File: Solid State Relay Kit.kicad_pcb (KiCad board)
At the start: 2 copper layers, 25.8 x 21 mm, 11 parts, among them J1 Conn_01x03, J2 Conn_01x02, Q1 2N3904, U1 S108T02

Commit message: update,
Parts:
- D1, D2: footprint LEDs:LED_0805_HandSoldering -> LED_SMD:LED_0805_2012Metric_Pad1.15x1.40mm_HandSolder
- J1: footprint footprint-lib:Pin_Header_Straight_1x03_Pitch2.54mm -> footprint-lib.pretty:Pin_Header_Straight_1x03_Pitch2.54mm
- Q1: footprint TO_SOT_Packages_SMD:TSOT-23_HandSoldering -> Package_TO_SOT_SMD:TSOT-23_HandSoldering
- R1, R2, R3, R4, R5: footprint Resistors_SMD:R_0805_HandSoldering -> footprint-lib.pretty:R_0805_HandSoldering

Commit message: update,
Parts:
- added REF**: MountingHole_3.2mm_M3, MountingHole:MountingHole_3.2mm_M3, F.Cu at (33.0, 21.6)
- added REF**: MountingHole_3.2mm_M3, MountingHole:MountingHole_3.2mm_M3, F.Cu at (33.0, 50.8)
- added REF**: MountingHole_3.2mm_M3, MountingHole:MountingHole_3.2mm_M3, F.Cu at (62.2, 21.6)
- added REF**: MountingHole_3.2mm_M3, MountingHole:MountingHole_3.2mm_M3, F.Cu at (62.2, 50.8)
- D1, D2: footprint LED_SMD:LED_0805_2012Metric_Pad1.15x1.40mm_HandSolder -> LED_SMD:LED_0805_2012Metric_Castellated
- J1: footprint footprint-lib.pretty:Pin_Header_Straight_1x03_Pitch2.54mm -> Connector_PinHeader_2.54mm:PinHeader_1x03_P2.54mm_Vertical
- J2: footprint Connectors_Phoenix:PhoenixContact_MCV-G_02x5.08mm_Vertical -> w_conn_mpt:mpt_0,5%2f2-2,54
- R1, R2, R3, R4, R5: footprint footprint-lib.pretty:R_0805_HandSoldering -> Resistor_SMD:R_0805_2012Metric_Pad1.15x1.40mm_HandSolder
- U1: footprint Housings_SIP:SIP4_Sharp-SSR_Pitch7.62mm_Straight -> footprint-lib:OMRON-G3MB-202P
- moved U1 18.5 mm to (55.9, 36.6), turned to 90 degrees
- moved D2 13.3 mm to (44.4, 41.3)
- moved R3 13.3 mm to (48.4, 42.1)
- moved R4 13.3 mm to (44.4, 36.3)
- moved R5 13.3 mm to (44.4, 44.0)
- moved R1 13.3 mm to (44.3, 34.1)
- moved R2 13.3 mm to (44.3, 31.9)
- moved D1 13.3 mm to (44.4, 39.0)
- moved Q1 13.3 mm to (49.1, 33.7)
- moved J1 10.5 mm to (32.0, 43.0)
- moved J2 8.29 mm to (33.5, 29.0), turned to 270 degrees
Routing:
- net GND: track 41.3 -> 49.6 mm
- net /SSR_OUT2: track 19.1 -> 24.4 mm
- net /SSR_IN1: track 19.7 -> 23.7 mm
- net /SSR_OUT1: track 22.1 -> 25.4 mm
- net +5V: track 13.6 -> 16.5 mm
- net /SSR_IN2: track 13.6 -> 16.4 mm
- net /SIG_CONTROL: track 12.3 -> 14.4 mm
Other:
- board size 25.8 x 21 mm -> 36.3 x 36.3 mm

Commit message: update,
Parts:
- added 5V1: TestPoint, TestPoint:TestPoint_Loop_D1.80mm_Drill1.0mm_Beaded, F.Cu at (49.5, 50.8)
- added C1: 105, Capacitor_SMD:CP_Elec_4x3, F.Cu at (36.6, 43.5)
- added D3: LED, LED_SMD:LED_0805_2012Metric_Castellated, F.Cu at (49.8, 46.4)
- added GND1: TestPoint, TestPoint:TestPoint_Loop_D1.80mm_Drill1.0mm_Beaded, F.Cu at (54.6, 50.8)
- added Q2: 2N3904, Package_TO_SOT_SMD:TSOT-23_HandSoldering, F.Cu at (55.2, 36.8)
- added R6: 331, Resistor_SMD:R_0805_2012Metric_Pad1.15x1.40mm_HandSolder, F.Cu at (49.8, 38.6)
- added R7: 103, Resistor_SMD:R_0805_2012Metric_Pad1.15x1.40mm_HandSolder, F.Cu at (49.8, 35.9)
- added R8: 331, Resistor_SMD:R_0805_2012Metric_Pad1.15x1.40mm_HandSolder, F.Cu at (49.8, 44.2)
- added R9: 680, Resistor_SMD:R_0805_2012Metric_Pad1.15x1.40mm_HandSolder, F.Cu at (49.8, 41.3)
- added SSR1: TestPoint, TestPoint:TestPoint_Loop_D1.80mm_Drill1.0mm_Beaded, F.Cu at (39.4, 50.9)
- added SSR2: TestPoint, TestPoint:TestPoint_Loop_D1.80mm_Drill1.0mm_Beaded, F.Cu at (44.5, 50.8)
- added U2: OMRON G3MB-202P, footprint-lib:OMRON-G3MB-202P, F.Cu at (50.0, 28.4)
- J1: footprint Connector_PinHeader_2.54mm:PinHeader_1x03_P2.54mm_Vertical -> Connector_PinHeader_2.54mm:PinHeader_1x04_P2.54mm_Vertical
- J2: value Conn_01x02 -> SSR_OUTPUT; footprint w_conn_mpt:mpt_0,5%2f2-2,54 -> w_conn_mpt:mpt_0,5%2f4-2,54
- R4: value 331 -> 680
- U1: value S108T02 -> OMRON G3MB-202P
- moved J2 35.4 mm to (67.3, 39.4), turned to 90 degrees
- moved R5 17.8 mm to (34.1, 29.5), turned to 270 degrees
- moved D2 17.6 mm to (31.4, 29.5), turned to 270 degrees
- moved U1 16.3 mm to (50.0, 21.3), turned to 0 degrees
- moved D1 7.31 mm to (43.5, 46.3)
- moved R1 6.88 mm to (39.2, 38.7)
- moved R2 6.64 mm to (39.2, 36.2)
- moved Q1 5.54 mm to (44.6, 36.8)
- moved R4 5.54 mm to (41.8, 41.2)
- moved REF** 5.33 mm to (67.6, 21.6)
- moved REF** 5.33 mm to (67.6, 50.8)
- moved R3 5.13 mm to (43.6, 43.8), turned to 180 degrees
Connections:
- net /SIG_CONTROL renamed /SSR_CONTROL1
- net /SSR_IN1 renamed /SSR1_IN1
- net /SSR_IN2 renamed /SSR1_IN2
- J2 pad 1: /SSR_OUT1 -> /SSR1_OUT2
- J2 pad 2: /SSR_OUT2 -> /SSR1_OUT1
- U1 pad 1: /SSR_OUT2 -> /SSR1_OUT2
- U1 pad 2: /SSR_OUT1 -> /SSR1_OUT1
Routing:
- net /SSR2_IN1: track 0.00 -> 39.1 mm, vias 0 -> 1
- net +5V: track 16.5 -> 52.6 mm
- net /SSR_CONTROL2: track 0.00 -> 32.1 mm, vias 0 -> 1
- net /SSR1_OUT1: track 0.00 -> 27.5 mm
- net /SSR_OUT1: track 25.4 -> 0.00 mm
- net /SSR_OUT2: track 24.4 -> 0.00 mm
- net /SSR2_OUT1: track 0.00 -> 23.5 mm
- net /SSR2_IN2: track 0.00 -> 19.8 mm, vias 0 -> 1
- net GND: track 49.6 -> 30.4 mm, vias 1 -> 4
- net /SSR1_OUT2: track 0.00 -> 16.9 mm
- net /SSR2_OUT2: track 0.00 -> 15.2 mm
- net /SSR_CONTROL1: track 14.4 -> 25.7 mm
- net Net-(Q2-Pad2): track 0.00 -> 10.9 mm
- net /SSR1_IN2: track 16.4 -> 26.6 mm
- net /SSR1_IN1: track 23.7 -> 31.2 mm
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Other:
- board size 36.3 x 36.3 mm -> 41.7 x 36.3 mm
- net class GND: via_dia 1 -> 1.4
- board text added: "MCU RELAY CONTROL BOARD"
- board text added: "ON = CLOSED OFF = OPEN"
- board text added: "PWR"
- board text added: "SSR1"
- board text added: "SSR2"

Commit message: update comment,
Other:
- board text added: "MCU RELAY CONTROL BOARD louiscklaw@gmail.com"
- board text removed: "MCU RELAY CONTROL BOARD"
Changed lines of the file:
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@@
     (pad 1 np_thru_hole circle (at 0 0) (size 3.2 3.2) (drill 3.2) (layers *.Cu *.Mask))
   )
-  (gr_text "MCU RELAY \nCONTROL BOARD" (at 62.484 34.8234) (layer B.SilkS)
-    (effects (font (size 1.5 1.5) (thickness 0.3)) (justify left mirror))
+  (gr_text "MCU RELAY \nCONTROL BOARD\n\nlouiscklaw@gmail.com" (at 62.738 38.608) (layer B.SilkS)
+    (effects (font (size 1.5 1.5) (thickness 0.2)) (justify left mirror))
   )
   (gr_text "ON = CLOSED\nOFF = OPEN" (at 59.7408 53.721 90) (layer F.SilkS)

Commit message: start panelizing,
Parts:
- removed the REF** at (33.0, 21.6)
- removed the REF** at (33.0, 50.8)
- removed the REF** at (67.6, 21.6)
- removed the REF** at (67.6, 50.8)
- added REF**: MountingHole_3.2mm_M3, MountingHole:MountingHole_3.2mm_M3, F.Cu at (5.02, 5.59)
- added REF**: MountingHole_3.2mm_M3, MountingHole:MountingHole_3.2mm_M3, F.Cu at (5.02, 34.8)
- added REF**: MountingHole_3.2mm_M3, MountingHole:MountingHole_3.2mm_M3, F.Cu at (39.6, 5.59)
- added REF**: MountingHole_3.2mm_M3, MountingHole:MountingHole_3.2mm_M3, F.Cu at (39.6, 34.8)
- moved SSR2 32.2 mm to (16.4, 34.8)
- moved 5V1 32.2 mm to (21.5, 34.8)
- moved C1 32.2 mm to (8.60, 27.5)
- moved D1 32.2 mm to (15.5, 30.3)
- moved D2 32.2 mm to (3.40, 13.5)
- moved D3 32.2 mm to (21.8, 30.4)
- moved GND1 32.2 mm to (26.6, 34.8)
- moved J1 32.2 mm to (4.00, 27.0)
- moved J2 32.2 mm to (39.3, 23.4)
- moved Q1 32.2 mm to (16.6, 20.8)
- moved Q2 32.2 mm to (27.2, 20.8)
- moved R1 32.2 mm to (11.2, 22.7)
- moved R2 32.2 mm to (11.2, 20.2)
- moved R3 32.2 mm to (15.6, 27.8)
- moved R4 32.2 mm to (13.8, 25.2)
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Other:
- board size 41.7 x 36.3 mm -> 90 x 90 mm

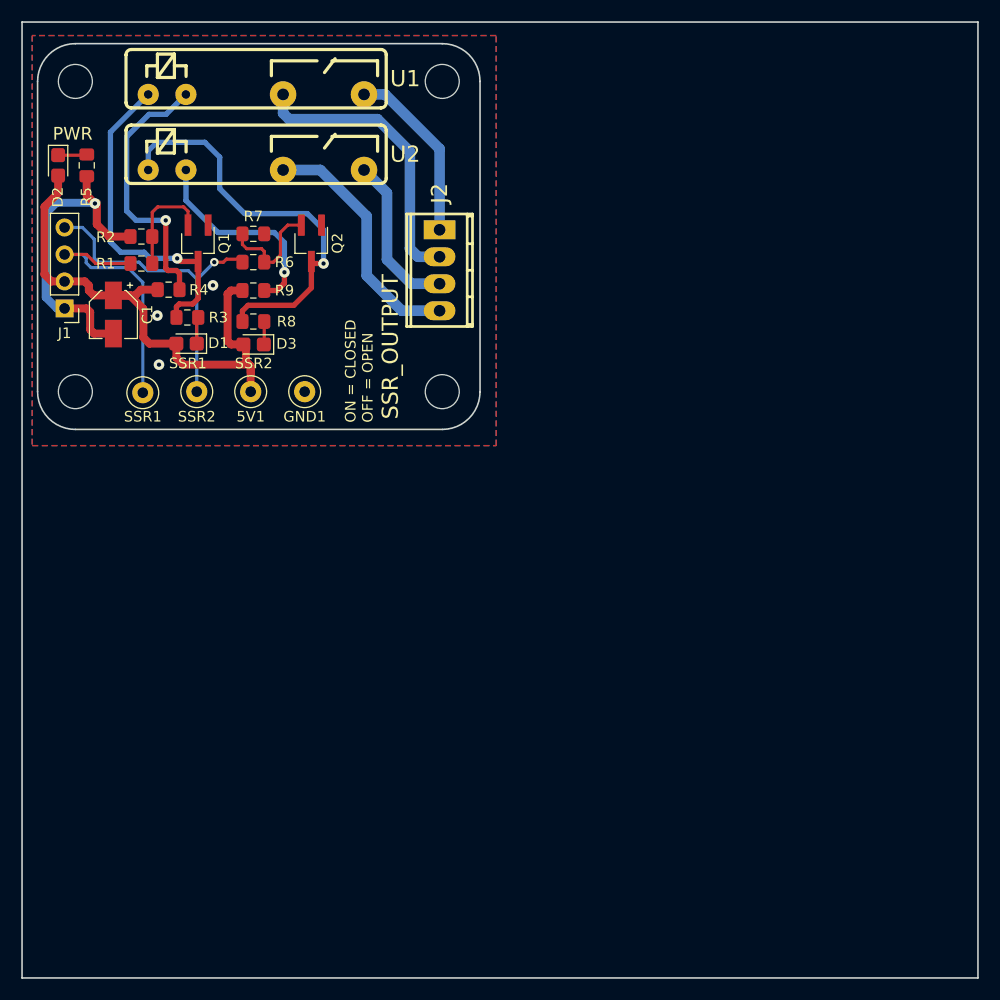
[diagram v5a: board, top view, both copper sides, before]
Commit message: simplify tracks,.
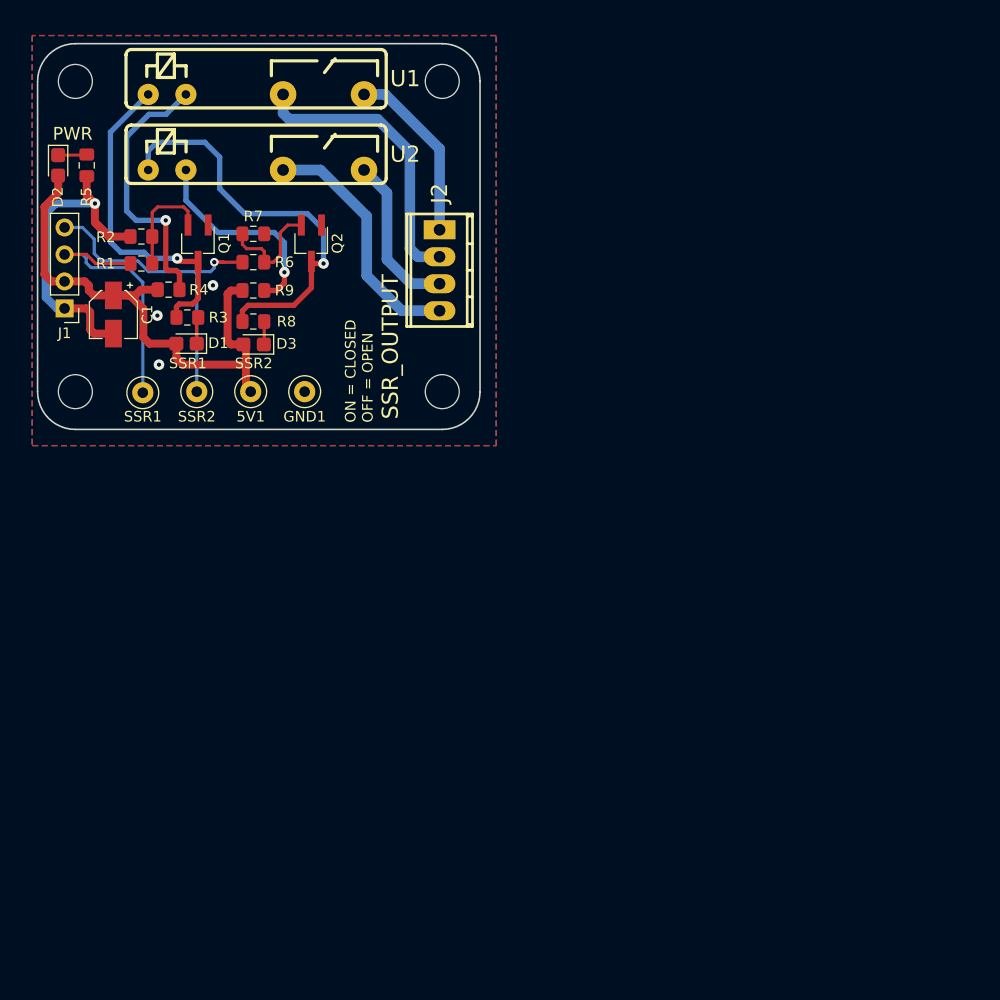
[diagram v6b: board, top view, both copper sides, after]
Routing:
- net GND: track 30.4 -> 31.9 mm
- net +5V: track 52.6 -> 51.6 mm
- net /SSR_CONTROL2: track 32.1 -> 33.0 mm
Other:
- board size 90 x 90 mm -> 41.7 x 36.3 mm
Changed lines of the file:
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@@
   (general
     (thickness 1.6)
-    (drawings 19)
-    (tracks 177)
+    (drawings 13)
+    (tracks 179)
     (zones 0)
     (modules 27)
@@
     (zone_45_only no)
     (trace_min 0.2)
-    (segment_width 0.2)
+    (segment_width 0.15)
     (edge_width 0.15)
     (via_size 0.8)
@@
     (pad 1 np_thru_hole circle (at 0 0) (size 3.2 3.2) (drill 3.2) (layers *.Cu *.Mask))
   )
-  (dimension 90 (width 0.3) (layer Dwgs.User)
-    (gr_text "90.000 mm" (at -5.1 45 270) (layer Dwgs.User)
-      (effects (font (size 1.5 1.5) (thickness 0.3)))
-    )
-    (feature1 (pts (xy 0 90) (xy -3.586421 90)))
-    (feature2 (pts (xy 0 0) (xy -3.586421 0)))
-    (crossbar (pts (xy -3 0) (xy -3 90)))
-    (arrow1a (pts (xy -3 90) (xy -3.586421 88.873496)))
-    (arrow1b (pts (xy -3 90) (xy -2.413579 88.873496)))
-    (arrow2a (pts (xy -3 0) (xy -3.586421 1.126504)))
-    (arrow2b (pts (xy -3 0) (xy -2.413579 1.126504)))
-  )
-  (dimension 90 (width 0.3) (layer Dwgs.User)
-    (gr_text "90.000 mm" (at 45 -5.1) (layer Dwgs.User)
-      (effects (font (size 1.5 1.5) (thickness 0.3)))
-    )
-    (feature1 (pts (xy 90 0) (xy 90 -3.586421)))
-    (feature2 (pts (xy 0 0) (xy 0 -3.586421)))
-    (crossbar (pts (xy 0 -3) (xy 90 -3)))
-    (arrow1a (pts (xy 90 -3) (xy 88.873496 -2.413579)))
-    (arrow1b (pts (xy 90 -3) (xy 88.873496 -3.586421)))
-    (arrow2a (pts (xy 0 -3) (xy 1.126504 -2.413579)))
-    (arrow2b (pts (xy 0 -3) (xy 1.126504 -3.586421)))
-  )
-  (gr_line (start 0 90) (end 0 0) (layer Edge.Cuts) (width 0.15))
-  (gr_line (start 90 90) (end 0 90) (layer Edge.Cuts) (width 0.15))
-  (gr_line (start 90 0) (end 90 90) (layer Edge.Cuts) (width 0.15))
-  (gr_line (start 0 0) (end 90 0) (layer Edge.Cuts) (width 0.15))
   (gr_text "MCU RELAY \nCONTROL BOARD\n\nlouiscklaw@gmail.com" (at 34.738 22.608) (layer B.SilkS)
     (effects (font (size 1.5 1.5) (thickness 0.2)) (justify left mirror))
@@
   (segment (start 6.29 25.275) (end 6.29 24.8034) (width 0.75) (layer F.Cu) (net 1))
   (segment (start 4.004 24.4224) (end 5.909 24.4224) (width 0.75) (layer F.Cu) (net 1))
-  (segment (start 21.53 34.8) (end 21.53 33.022) (width 0.75) (layer F.Cu) (net 1))
-  (segment (start 15.18 32.26) (end 14.525 31.605) (width 0.75) (layer F.Cu) (net 1))
-  (segment (start 21.276 32.26) (end 15.18 32.26) (width 0.75) (layer F.Cu) (net 1))
-  (segment (start 14.525 31.605) (end 14.525 30.2788) (width 0.75) (layer F.Cu) (net 1))
-  (segment (start 21.53 33.022) (end 21.53 32.514) (width 0.75) (layer F.Cu) (net 1))
-  (segment (start 21.53 32.514) (end 21.276 32.26) (width 0.75) (layer F.Cu) (net 1))
   (segment (start 2.11401 23.76601) (end 2.7704 24.4224) (width 0.75) (layer F.Cu) (net 1))
   (segment (start 2.7704 24.4224) (end 4.004 24.4224) (width 0.75) (layer F.Cu) (net 1))
@@
   (segment (start 3.39792 14.457044) (end 3.39792 16.10208) (width 0.75) (layer F.Cu) (net 1))
   (segment (start 3.39792 16.10208) (end 2.11401 17.38599) (width 0.75) (layer F.Cu) (net 1))
-  (segment (start 21.53 32.387) (end 21.0755 31.9325) (width 0.75) (layer F.Cu) (net 1))
-  (segment (start 21.53 33.022) (end 21.53 32.387) (width 0.75) (layer F.Cu) (net 1))
   (segment (start 21.0755 31.9325) (end 21.0755 30.355) (width 0.75) (layer F.Cu) (net 1))
   (segment (start 19.6758 25.275) (end 20.75 25.275) (width 0.75) (layer F.Cu) (net 1))
@@
   (segment (start 8.6014 25.7356) (end 10.1514 25.7356) (width 0.75) (layer F.Cu) (net 1))
   (segment (start 10.1514 25.7356) (end 11.4208 27.005) (width 0.75) (layer F.Cu) (net 1))
+  (segment (start 21.0755 34.3455) (end 21.53 34.8) (width 0.75) (layer F.Cu) (net 1))
+  (segment (start 14.525 31.605) (end 15.18 32.26) (width 0.75) (layer F.Cu) (net 1))
+  (segment (start 14.525 30.2788) (end 14.525 31.605) (width 0.75) (layer F.Cu) (net 1))
+  (segment (start 21.0655 32.26) (end 21.0755 32.25) (width 0.75) (layer F.Cu) (net 1))
+  (segment (start 15.18 32.26) (end 21.0655 32.26) (width 0.75) (layer F.Cu) (net 1))
+  (segment (start 21.0755 31.9325) (end 21.0755 32.25) (width 0.75) (layer F.Cu) (net 1))
+  (segment (start 21.0755 32.25) (end 21.0755 34.3455) (width 0.75) (layer F.Cu) (net 1))
   (segment (start 16.45 27.2308) (end 16.45 29.748366) (width 0.3) (layer F.Cu) (net 2) (status 30))
   (segment (start 16.45 29.748366) (end 16.5825 29.880866) (width 0.3) (layer F.Cu) (net 2) (status 30))
   (segment (start 10.209 20.195) (end 8.195 20.195) (width 0.75) (layer F.Cu) (net 3))
-  (segment (start 7.034 19.034) (end 7.034 17.02) (width 0.75) (layer F.Cu) (net 3))
   (segment (start 8.195 20.195) (end 7.034 19.034) (width 0.75) (layer F.Cu) (net 3))
   (segment (start 6.7946 29.3356) (end 8.6014 29.3356) (width 0.75) (layer F.Cu) (net 3))
@@
   (segment (start 4.004 26.9624) (end 3.2784 26.9624) (width 0.75) (layer B.Cu) (net 3))
   (segment (start 3.2784 26.9624) (end 2.226 25.91) (width 0.75) (layer B.Cu) (net 3))
-  (segment (start 3.242 17.02) (end 2.226 18.036) (width 0.75) (layer B.Cu) (net 3))
   (segment (start 2.226 25.91) (end 2.226 18.036) (width 0.75) (layer B.Cu) (net 3))
-  (segment (start 7.052 17.02) (end 3.242 17.02) (width 0.75) (layer B.Cu) (net 3))
   (via (at 12.894 32.26) (size 1) (drill 0.4) (layers F.Cu B.Cu) (net 3))
-  (segment (start 7.034 17.02) (end 7.034 17.02) (width 0.75) (layer F.Cu) (net 3))
   (segment (start 6.09032 16.31232) (end 6.8615 17.0835) (width 0.75) (layer F.Cu) (net 3))
   (segment (start 6.09032 14.519544) (end 6.09032 16.31232) (width 0.75) (layer F.Cu) (net 3))
@@
   (via (at 17.974 24.7924) (size 1) (drill 0.4) (layers F.Cu B.Cu) (net 3))
   (via (at 12.7416 27.6372) (size 1) (drill 0.4) (layers F.Cu B.Cu) (net 3))
+  (segment (start 6.8615 18.8615) (end 8.195 20.195) (width 0.75) (layer F.Cu) (net 3))
+  (segment (start 6.8615 17.0835) (end 6.8615 18.8615) (width 0.75) (layer F.Cu) (net 3))
+  (segment (start 3.1785 17.0835) (end 2.226 18.036) (width 0.75) (layer B.Cu) (net 3))
+  (segment (start 6.8615 17.0835) (end 3.1785 17.0835) (width 0.75) (layer B.Cu) (net 3))
   (segment (start 12.259 20.195) (end 12.259 22.735) (width 0.3) (layer F.Cu) (net 4) (status 30))
   (segment (start 15.627 17.82) (end 15.208 17.401) (width 0.3) (layer F.Cu) (net 4))
@@
   (via (at 18.101 22.608) (size 0.8) (drill 0.4) (layers F.Cu B.Cu) (net 7))
   (segment (start 18.101 22.608) (end 18.96075 22.608) (width 0.3) (layer F.Cu) (net 7))
-  (segment (start 18.96075 22.608) (end 19.244 22.32475) (width 0.3) (layer F.Cu) (net 7))
-  (segment (start 20.75 22.32475) (end 19.244 22.32475) (width 0.3) (layer F.Cu) (net 7))
   (segment (start 16.45 31.244) (end 16.45 34.8) (width 0.3) (layer B.Cu) (net 7))
-  (segment (start 16.45 24.259) (end 18.101 22.608) (width 0.3) (layer B.Cu) (net 7))
   (segment (start 16.45 25.1861) (end 16.45 24.259) (width 0.3) (layer B.Cu) (net 7))
   (segment (start 16.45 25.1861) (end 16.45 31.244) (width 0.3) (layer B.Cu) (net 7))
-  (segment (start 5.6914 19.3424) (end 4.004 19.3424) (width 0.3) (layer B.Cu) (net 7))
-  (segment (start 6.798 20.449) (end 5.6914 19.3424) (width 0.3) (layer B.Cu) (net 7))
-  (segment (start 16.45 25.1861) (end 16.45 24.1955) (width 0.3) (layer B.Cu) (net 7))
-  (segment (start 6.798 22.227) (end 6.798 20.449) (width 0.3) (layer B.Cu) (net 7))
-  (segment (start 16.45 24.1955) (end 15.6626 23.4081) (width 0.3) (layer B.Cu) (net 7))
-  (segment (start 11.8145 23.4081) (end 11.0144 22.608) (width 0.3) (layer B.Cu) (net 7))
-  (segment (start 15.6626 23.4081) (end 11.8145 23.4081) (width 0.3) (layer B.Cu) (net 7))
-  (segment (start 7.179 22.608) (end 6.798 22.227) (width 0.3) (layer B.Cu) (net 7))
-  (segment (start 11.0144 22.608) (end 7.179 22.608) (width 0.3) (layer B.Cu) (net 7))
+  (segment (start 16.45 24.5) (end 16.45 25.1861) (width 0.3) (layer B.Cu) (net 7))
+  (segment (start 16.45 23.7) (end 16.45 24.5) (width 0.3) (layer B.Cu) (net 7))
+  (segment (start 16.65 23.5) (end 16.45 23.7) (width 0.3) (layer B.Cu) (net 7))
+  (segment (start 18.101 22.608) (end 18.101 23.149) (width 0.3) (layer B.Cu) (net 7))
+  (segment (start 17.75 23.5) (end 16.65 23.5) (width 0.3) (layer B.Cu) (net 7))
+  (segment (start 18.101 23.149) (end 17.75 23.5) (width 0.3) (layer B.Cu) (net 7))
+  (segment (start 11.9064 23.5) (end 16.25 23.5) (width 0.3) (layer B.Cu) (net 7))
+  (segment (start 5.6914 19.3424) (end 6.798 20.449) (width 0.3) (layer B.Cu) (net 7))
+  (segment (start 16.25 23.5) (end 16.45 23.7) (width 0.3) (layer B.Cu) (net 7))
+  (segment (start 6.798 20.449) (end 6.798 21.798) (width 0.3) (layer B.Cu) (net 7))
+  (segment (start 4.004 19.3424) (end 5.6914 19.3424) (width 0.3) (layer B.Cu) (net 7))
+  (segment (start 6.798 21.798) (end 7.5 22.5) (width 0.3) (layer B.Cu) (net 7))
+  (segment (start 7.5 22.5) (end 10.9064 22.5) (width 0.3) (layer B.Cu) (net 7))
+  (segment (start 10.9064 22.5) (end 11.9064 23.5) (width 0.3) (layer B.Cu) (net 7))
+  (segment (start 18.101 22.608) (end 20.75 22.608) (width 0.3) (layer F.Cu) (net 7))
   (segment (start 6.0724 21.8824) (end 6.925 22.735) (width 0.3) (layer F.Cu) (net 8))
   (segment (start 6.925 22.735) (end 10.209 22.735) (width 0.3) (layer F.Cu) (net 8) (status 20))
